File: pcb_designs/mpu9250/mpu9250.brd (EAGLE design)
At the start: 27.9 x 14.9 mm, 2 parts

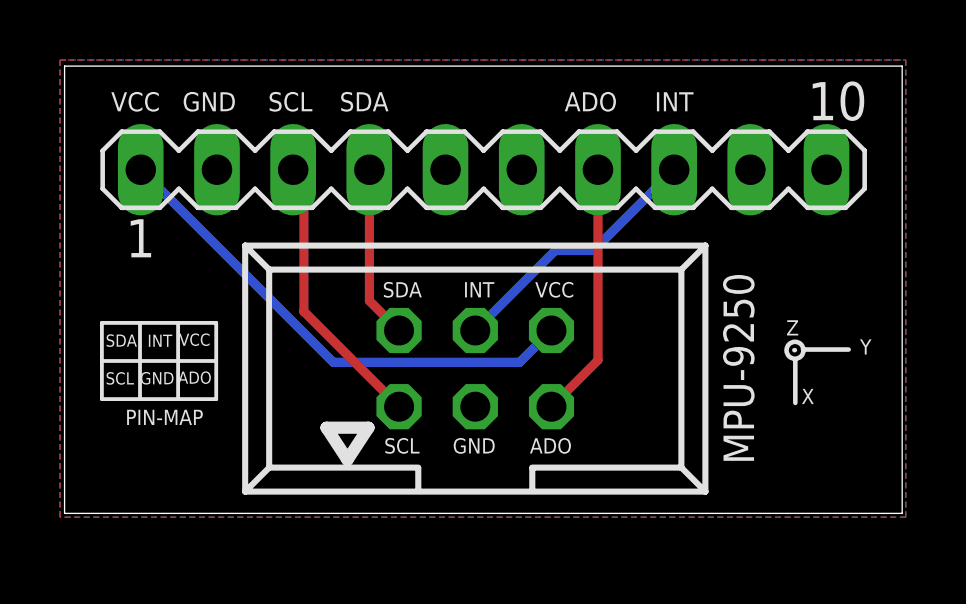
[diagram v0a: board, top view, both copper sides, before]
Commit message: Added BNO055 MPU files
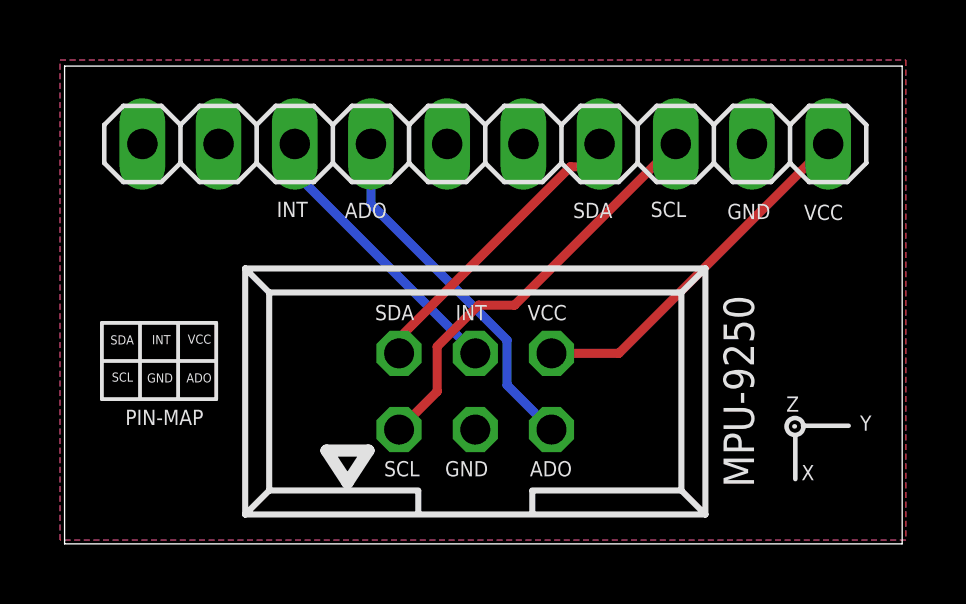
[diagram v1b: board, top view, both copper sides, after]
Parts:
- removed JP1: (no value), con-lstb:MA10-1
- added JP2: (no value), pinhead:1X10
- moved MPU-9250 0.76 mm to (11.2, 4.06)
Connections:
- net AD0: now also JP2.4; no longer JP1.7
- net ECL: now also JP2.5; no longer JP1.6
- net EDA: now also JP2.6; no longer JP1.5
- net FSYNC: now also JP2.1; no longer JP1.10
- net GND: now also JP2.9; no longer JP1.2
- net INT: now also JP2.3; no longer JP1.8
- net NCS: now also JP2.2; no longer JP1.9
- net SCL: now also JP2.8; no longer JP1.3
- net SDA: now also JP2.7; no longer JP1.4
- net VCC: now also JP2.10; no longer JP1.1
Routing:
- net SCL: track 9.36 -> 14.0 mm
- net VCC: track 16.8 -> 12.1 mm
- net SDA: track 5.77 -> 10.3 mm
- net AD0: track 8.54 -> 12.0 mm
- net INT: track 8.85 -> 9.47 mm
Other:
- board size 27.9 x 14.9 mm -> 27.9 x 15.9 mm
